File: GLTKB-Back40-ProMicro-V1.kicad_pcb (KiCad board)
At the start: 2 copper layers, 142.9 x 145.3 mm, 98 parts, among them K0 KEYSW, K1 KEYSW, K2 KEYSW, K3 KEYSW, K4 KEYSW, K5 KEYSW, K6 KEYSW, K7 KEYSW, K8 KEYSW, K9 KEYSW, U1 ProMicro

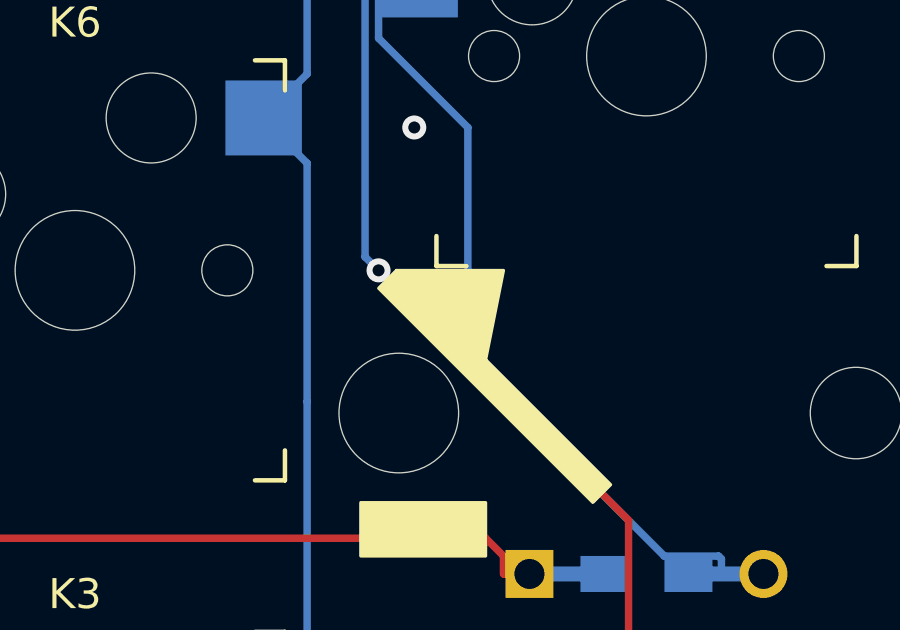
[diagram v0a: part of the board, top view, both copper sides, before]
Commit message: Removed uneeded front silk trace protector, since it wasn't protecting a front side trace.
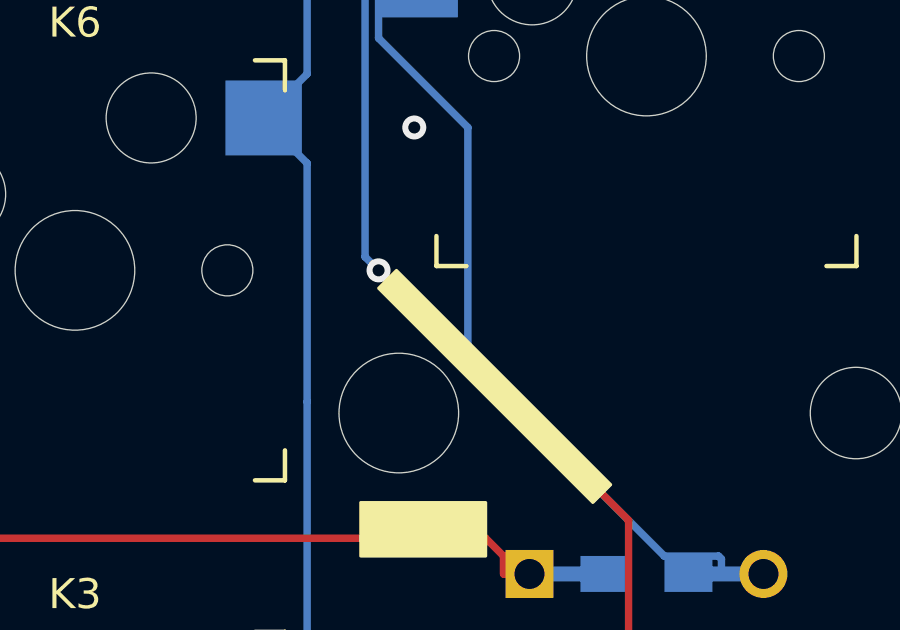
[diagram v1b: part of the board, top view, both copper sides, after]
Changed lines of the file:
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@@
   (general
     (thickness 1.6)
-    (drawings 358)
+    (drawings 357)
     (tracks 646)
     (zones 0)
@@
     )
   )
-  (gr_poly (pts (xy 158.948571 117.276661) (xy 155.972006 114.300096) (xy 159.543884 114.300096)) (layer F.SilkS) (width 0.1))
   (gr_poly (pts (xy 163.115762 121.443852) (xy 162.520449 122.039165) (xy 155.376693 114.895409) (xy 155.972006 114.300096)) (layer F.SilkS) (width 0.1))
   (gr_text "GeekLab Technologies GLTKB-Back-40%-Pro-Micro V1.0.0" (at 135.731364 44.648475) (layer F.SilkS)

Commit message: Move some mounting holes.
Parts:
- removed the REF** at (145.3, 157.2)
- removed the REF** at (145.3, 61.9)
- removed the REF** at (145.3, 100.0)
- added REF**: M2, Mounting_Holes:MountingHole_2.2mm_M2, F.Cu at (116.7, 157.2)
- added REF**: M2, Mounting_Holes:MountingHole_2.2mm_M2, F.Cu at (126.2, 59.5)
- added REF**: M2, Mounting_Holes:MountingHole_2.2mm_M2, F.Cu at (126.2, 97.6)
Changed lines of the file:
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@@
   )
   (module Mounting_Holes:MountingHole_2.2mm_M2 (layer F.Cu)
-    (at 145.256908 157.162784)
+    (at 116.681348 157.162632)
     (descr "Mounting Hole 2.2mm, no annular, M2")
     (tags "mounting hole 2.2mm no annular m2")
@@
   )
   (module Mounting_Holes:MountingHole_2.2mm_M2 (layer F.Cu)
-    (at 145.256908 61.912704)
+    (at 126.206356 59.5313)
     (descr "Mounting Hole 2.2mm, no annular, M2")
     (tags "mounting hole 2.2mm no annular m2")
@@
   )
   (module Mounting_Holes:MountingHole_2.2mm_M2 (layer F.Cu)
-    (at 145.256908 100.012736)
+    (at 126.206356 97.631332)
     (descr "Mounting Hole 2.2mm, no annular, M2")
     (tags "mounting hole 2.2mm no annular m2")
